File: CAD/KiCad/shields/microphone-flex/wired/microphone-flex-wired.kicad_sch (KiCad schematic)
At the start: 22 parts, among them J1 GND / +5V / OUT, J2 LEFT / 1x05 RIGHT ANGLE, J3 RIGHT / 1x05 RIGHT ANGLE, M1 UP / ONE MODULE ONLY

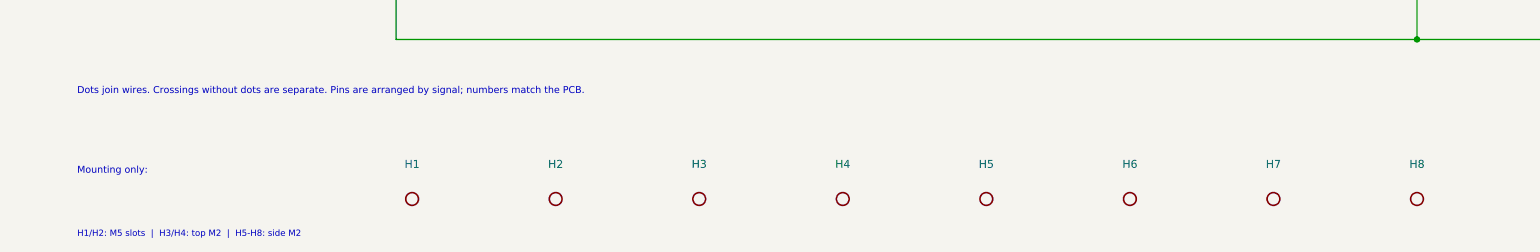
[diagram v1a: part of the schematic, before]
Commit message: Reroute microphone flex around the approved component placement
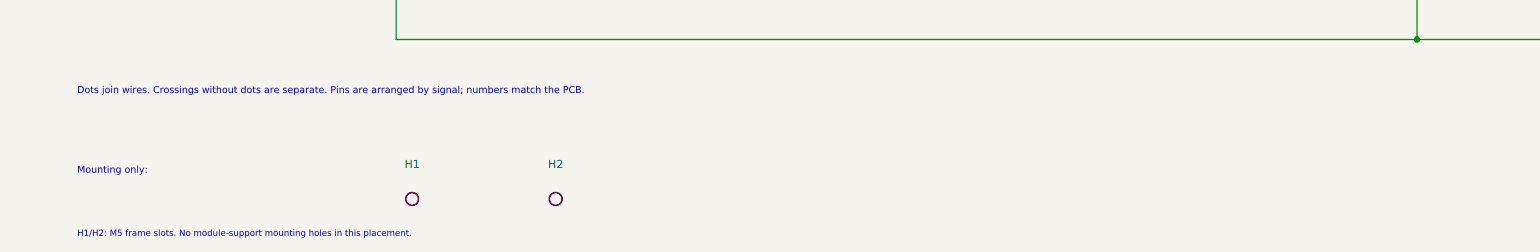
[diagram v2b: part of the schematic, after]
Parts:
- removed H3: M2 MODULE / INSULATING SPACER, Shields:Flex_M2_Top, symbol Colloquy:H3
- removed H4: M2 MODULE / INSULATING SPACER, Shields:Flex_M2_Top, symbol Colloquy:H4
- removed H5: M2 SIDE SUPPORT BASE, Shields:Flex_M2_Base, symbol Colloquy:H5
- removed H6: M2 SIDE SUPPORT BASE, Shields:Flex_M2_Base, symbol Colloquy:H6
- removed H7: M2 SIDE SUPPORT BASE, Shields:Flex_M2_Base, symbol Colloquy:H7
- removed H8: M2 SIDE SUPPORT BASE, Shields:Flex_M2_Base, symbol Colloquy:H8
- J2: footprint Shields:Flex_Socket_Side -> Shields:Flex_Socket_Left_Overhang
- J3: footprint Shields:Flex_Socket_Side -> Shields:Flex_Socket_Right_Overhang
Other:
- note added: "H1/H2: M5 frame slots. No module-support mounting holes in this placement."
- note removed: "H1/H2: M5 slots | H3/H4: top M2 | H5-H8: side M2"
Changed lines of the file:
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@@
 (symbol (lib_id "Colloquy:M1") (at 182.88 68.58 0) (unit 1) (in_bom yes) (on_board yes)(property "Reference" "M1" (at 182.8800 55.4200 0) (effects (font (size 1.27 1.27))  ))(property "Value" "UP / ONE MODULE ONLY" (at 182.8800 68.5800 0) (effects (font (size 1.27 1.27))  (hide yes)))(property "Footprint" "Shields:Flex_Socket_Up" (at 182.8800 68.5800 0) (effects (font (size 1.27 1.27))  (hide yes)))(instances (project "microphone-flex-wired" (path "/cd62561b-1660-5a82-97f3-9afdea717d34" (reference "M1") (unit 1)))))
 (text "UP / vertical" (at 157.48 60.96 0) (effects (font (size 1.27 1.27) ) (justify left top)))
-(symbol (lib_id "Colloquy:J2") (at 261.62 68.58 0) (unit 1) (in_bom yes) (on_board yes)(property "Reference" "J2" (at 261.6200 55.4200 0) (effects (font (size 1.27 1.27))  ))(property "Value" "LEFT / 1x05 RIGHT ANGLE" (at 261.6200 68.5800 0) (effects (font (size 1.27 1.27))  (hide yes)))(property "Footprint" "Shields:Flex_Socket_Side" (at 261.6200 68.5800 0) (effects (font (size 1.27 1.27))  (hide yes)))(instances (project "microphone-flex-wired" (path "/cd62561b-1660-5a82-97f3-9afdea717d34" (reference "J2") (unit 1)))))
+(symbol (lib_id "Colloquy:J2") (at 261.62 68.58 0) (unit 1) (in_bom yes) (on_board yes)(property "Reference" "J2" (at 261.6200 55.4200 0) (effects (font (size 1.27 1.27))  ))(property "Value" "LEFT / 1x05 RIGHT ANGLE" (at 261.6200 68.5800 0) (effects (font (size 1.27 1.27))  (hide yes)))(property "Footprint" "Shields:Flex_Socket_Left_Overhang" (at 261.6200 68.5800 0) (effects (font (size 1.27 1.27))  (hide yes)))(instances (project "microphone-flex-wired" (path "/cd62561b-1660-5a82-97f3-9afdea717d34" (reference "J2") (unit 1)))))
 (text "LEFT / right angle" (at 236.22 60.96 0) (effects (font (size 1.27 1.27) ) (justify left top)))
-(symbol (lib_id "Colloquy:J3") (at 340.36 68.58 0) (unit 1) (in_bom yes) (on_board yes)(property "Reference" "J3" (at 340.3600 55.4200 0) (effects (font (size 1.27 1.27))  ))(property "Value" "RIGHT / 1x05 RIGHT ANGLE" (at 340.3600 68.5800 0) (effects (font (size 1.27 1.27))  (hide yes)))(property "Footprint" "Shields:Flex_Socket_Side" (at 340.3600 68.5800 0) (effects (font (size 1.27 1.27))  (hide yes)))(instances (project "microphone-flex-wired" (path "/cd62561b-1660-5a82-97f3-9afdea717d34" (reference "J3") (unit 1)))))
+(symbol (lib_id "Colloquy:J3") (at 340.36 68.58 0) (unit 1) (in_bom yes) (on_board yes)(property "Reference" "J3" (at 340.3600 55.4200 0) (effects (font (size 1.27 1.27))  ))(property "Value" "RIGHT / 1x05 RIGHT ANGLE" (at 340.3600 68.5800 0) (effects (font (size 1.27 1.27))  (hide yes)))(property "Footprint" "Shields:Flex_Socket_Right_Overhang" (at 340.3600 68.5800 0) (effects (font (size 1.27 1.27))  (hide yes)))(instances (project "microphone-flex-wired" (path "/cd62561b-1660-5a82-97f3-9afdea717d34" (reference "J3") (unit 1)))))
 (text "RIGHT / right angle" (at 314.96 60.96 0) (effects (font (size 1.27 1.27) ) (justify left top)))
 (symbol (lib_id "Colloquy:J1") (at 30.48 142.24 0) (unit 1) (in_bom yes) (on_board yes)(property "Reference" "J1" (at 30.4800 88.4400 0) (effects (font (size 1.27 1.27))  ))(property "Value" "GND / +5V / OUT" (at 30.4800 142.2400 0) (effects (font (size 1.27 1.27))  (hide yes)))(property "Footprint" "Shields:JST_EH_B3B-EH-A_1x03_P2.50mm_Vertical" (at 30.4800 142.2400 0) (effects (font (size 1.27 1.27))  (hide yes)))(instances (project "microphone-flex-wired" (path "/cd62561b-1660-5a82-97f3-9afdea717d34" (reference "J1") (unit 1)))))
@@
 (symbol (lib_id "Colloquy:H1") (at 73.66 274.32 0) (unit 1) (in_bom no) (on_board yes)(property "Reference" "H1" (at 73.6600 268.7800 0) (effects (font (size 1.27 1.27))  ))(property "Value" "M5 SLOT 12x5.5 / TRANSVERSE" (at 73.6600 274.3200 0) (effects (font (size 1.27 1.27))  (hide yes)))(property "Footprint" "Shields:Flex_M5_Slot12x5.5_Keepout" (at 73.6600 274.3200 0) (effects (font (size 1.27 1.27))  (hide yes)))(instances (project "microphone-flex-wired" (path "/cd62561b-1660-5a82-97f3-9afdea717d34" (reference "H1") (unit 1)))))
 (symbol (lib_id "Colloquy:H2") (at 96.52 274.32 0) (unit 1) (in_bom no) (on_board yes)(property "Reference" "H2" (at 96.5200 268.7800 0) (effects (font (size 1.27 1.27))  ))(property "Value" "M5 SLOT 12x5.5 / TRANSVERSE" (at 96.5200 274.3200 0) (effects (font (size 1.27 1.27))  (hide yes)))(property "Footprint" "Shields:Flex_M5_Slot12x5.5_Keepout" (at 96.5200 274.3200 0) (effects (font (size 1.27 1.27))  (hide yes)))(instances (project "microphone-flex-wired" (path "/cd62561b-1660-5a82-97f3-9afdea717d34" (reference "H2") (unit 1)))))
-(symbol (lib_id "Colloquy:H3") (at 119.38 274.32 0) (unit 1) (in_bom no) (on_board yes)(property "Reference" "H3" (at 119.3800 268.7800 0) (effects (font (size 1.27 1.27))  ))(property "Value" "M2 MODULE / INSULATING SPACER" (at 119.3800 274.3200 0) (effects (font (size 1.27 1.27))  (hide yes)))(property "Footprint" "Shields:Flex_M2_Top" (at 119.3800 274.3200 0) (effects (font (size 1.27 1.27))  (hide yes)))(instances (project "microphone-flex-wired" (path "/cd62561b-1660-5a82-97f3-9afdea717d34" (reference "H3") (unit 1)))))
-(symbol (lib_id "Colloquy:H4") (at 142.24 274.32 0) (unit 1) (in_bom no) (on_board yes)(property "Reference" "H4" (at 142.2400 268.7800 0) (effects (font (size 1.27 1.27))  ))(property "Value" "M2 MODULE / INSULATING SPACER" (at 142.2400 274.3200 0) (effects (font (size 1.27 1.27))  (hide yes)))(property "Footprint" "Shields:Flex_M2_Top" (at 142.2400 274.3200 0) (effects (font (size 1.27 1.27))  (hide yes)))(instances (project "microphone-flex-wired" (path "/cd62561b-1660-5a82-97f3-9afdea717d34" (reference "H4") (unit 1)))))
-(symbol (lib_id "Colloquy:H5") (at 165.1 274.32 0) (unit 1) (in_bom no) (on_board yes)(property "Reference" "H5" (at 165.1000 268.7800 0) (effects (font (size 1.27 1.27))  ))(property "Value" "M2 SIDE SUPPORT BASE" (at 165.1000 274.3200 0) (effects (font (size 1.27 1.27))  (hide yes)))(property "Footprint" "Shields:Flex_M2_Base" (at 165.1000 274.3200 0) (effects (font (size 1.27 1.27))  (hide yes)))(instances (project "microphone-flex-wired" (path "/cd62561b-1660-5a82-97f3-9afdea717d34" (reference "H5") (unit 1)))))
-(symbol (lib_id "Colloquy:H6") (at 187.96 274.32 0) (unit 1) (in_bom no) (on_board yes)(property "Reference" "H6" (at 187.9600 268.7800 0) (effects (font (size 1.27 1.27))  ))(property "Value" "M2 SIDE SUPPORT BASE" (at 187.9600 274.3200 0) (effects (font (size 1.27 1.27))  (hide yes)))(property "Footprint" "Shields:Flex_M2_Base" (at 187.9600 274.3200 0) (effects (font (size 1.27 1.27))  (hide yes)))(instances (project "microphone-flex-wired" (path "/cd62561b-1660-5a82-97f3-9afdea717d34" (reference "H6") (unit 1)))))
-(symbol (lib_id "Colloquy:H7") (at 210.82 274.32 0) (unit 1) (in_bom no) (on_board yes)(property "Reference" "H7" (at 210.8200 268.7800 0) (effects (font (size 1.27 1.27))  ))(property "Value" "M2 SIDE SUPPORT BASE" (at 210.8200 274.3200 0) (effects (font (size 1.27 1.27))  (hide yes)))(property "Footprint" "Shields:Flex_M2_Base" (at 210.8200 274.3200 0) (effects (font (size 1.27 1.27))  (hide yes)))(instances (project "microphone-flex-wired" (path "/cd62561b-1660-5a82-97f3-9afdea717d34" (reference "H7") (unit 1)))))
-(symbol (lib_id "Colloquy:H8") (at 233.68 274.32 0) (unit 1) (in_bom no) (on_board yes)(property "Reference" "H8" (at 233.6800 268.7800 0) (effects (font (size 1.27 1.27))  ))(property "Value" "M2 SIDE SUPPORT BASE" (at 233.6800 274.3200 0) (effects (font (size 1.27 1.27))  (hide yes)))(property "Footprint" "Shields:Flex_M2_Base" (at 233.6800 274.3200 0) (effects (font (size 1.27 1.27))  (hide yes)))(instances (project "microphone-flex-wired" (path "/cd62561b-1660-5a82-97f3-9afdea717d34" (reference "H8") (unit 1)))))
-(text "H1/H2: M5 slots  |  H3/H4: top M2  |  H5-H8: side M2" (at 20.32 279.4 0) (effects (font (size 1.0 1.0) ) (justify left top)))
+(text "H1/H2: M5 frame slots. No module-support mounting holes in this placement." (at 20.32 279.4 0) (effects (font (size 1.0 1.0) ) (justify left top)))
 (wire (pts (xy 55.8800 101.6000) (xy 66.0400 101.6000)) (stroke (width 0) (type default)))
 (wire (pts (xy 55.8800 162.5600) (xy 83.8200 162.5600)) (stroke (width 0) (type default)))

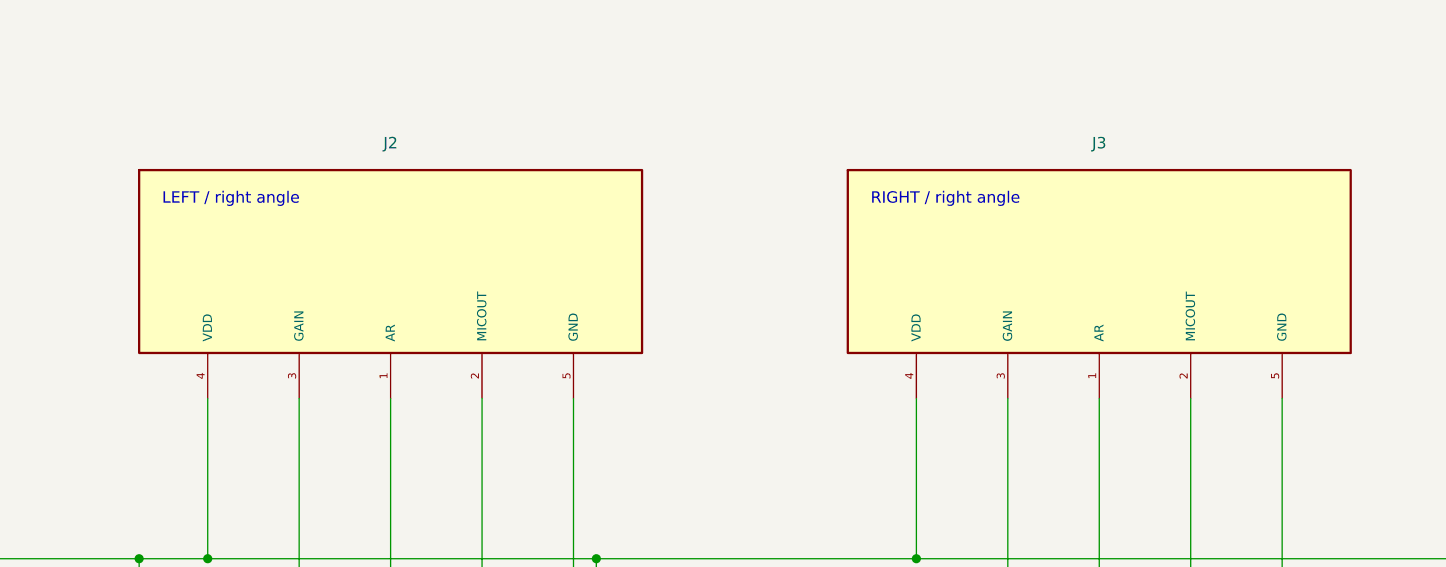
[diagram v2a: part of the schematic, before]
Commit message: Flip side microphones below the carrier and reverse their pin mapping
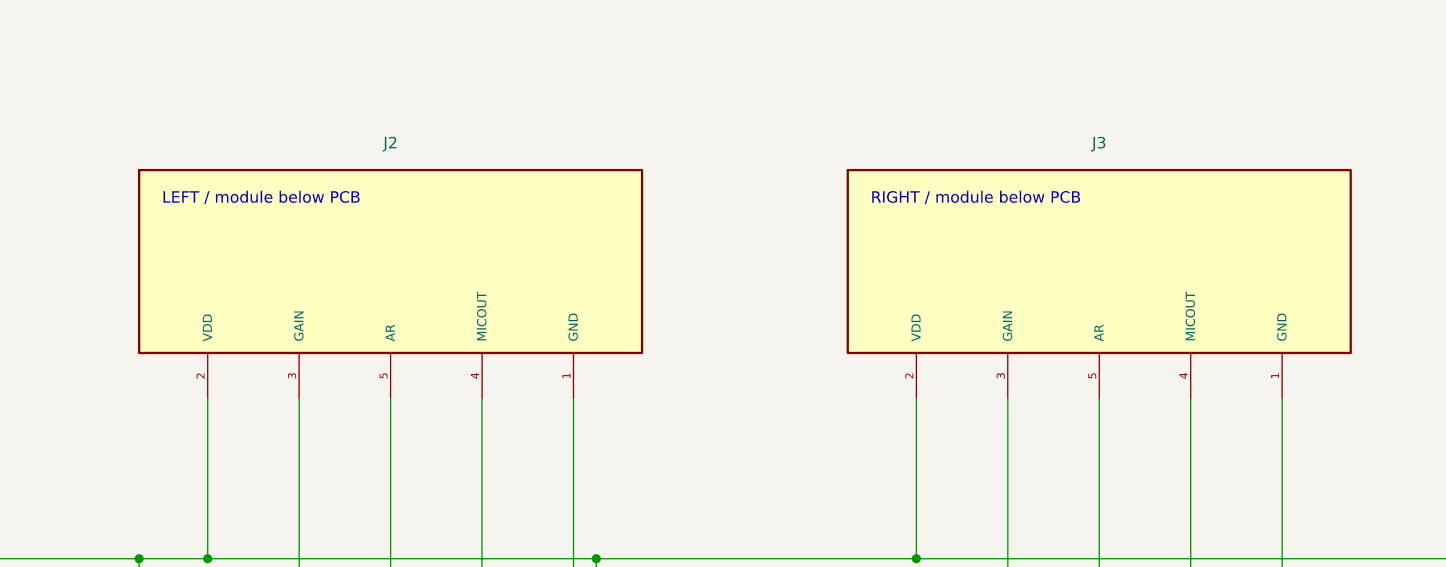
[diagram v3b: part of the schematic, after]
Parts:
- J2: value LEFT / 1x05 RIGHT ANGLE -> LEFT / DOWNWARD MODULE
- J3: value RIGHT / 1x05 RIGHT ANGLE -> RIGHT / DOWNWARD MODULE
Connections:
- net at C6.1, C7.1, JP1.3 (VDD)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: now also J2.2 (VDD), J3.2 (VDD); no longer J2.4 (VDD), J3.4 (VDD)
- net at C6.2, C7.2, D1.1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: now also J2.1 (GND), J3.1 (GND); no longer J2.5 (GND), J3.5 (GND)
- net at M1.4 (Out), R5.1, TP1.1: now also J2.4 (MICOUT), J3.4 (MICOUT); no longer J2.2 (MICOUT), J3.2 (MICOUT)
- net at JP2.2 (AR), M1.5 (AR): now also J2.5 (AR), J3.5 (AR); no longer J2.1 (AR), J3.1 (AR)
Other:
- note added: "LEFT / module below PCB"
- note added: "RIGHT / module below PCB"
- note removed: "LEFT / right angle"
- note removed: "RIGHT / right angle"
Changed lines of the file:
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@@
 (symbol (lib_id "Colloquy:M1") (at 182.88 68.58 0) (unit 1) (in_bom yes) (on_board yes)(property "Reference" "M1" (at 182.8800 55.4200 0) (effects (font (size 1.27 1.27))  ))(property "Value" "UP / ONE MODULE ONLY" (at 182.8800 68.5800 0) (effects (font (size 1.27 1.27))  (hide yes)))(property "Footprint" "Shields:Flex_Socket_Up" (at 182.8800 68.5800 0) (effects (font (size 1.27 1.27))  (hide yes)))(instances (project "microphone-flex-wired" (path "/cd62561b-1660-5a82-97f3-9afdea717d34" (reference "M1") (unit 1)))))
 (text "UP / vertical" (at 157.48 60.96 0) (effects (font (size 1.27 1.27) ) (justify left top)))
-(symbol (lib_id "Colloquy:J2") (at 261.62 68.58 0) (unit 1) (in_bom yes) (on_board yes)(property "Reference" "J2" (at 261.6200 55.4200 0) (effects (font (size 1.27 1.27))  ))(property "Value" "LEFT / 1x05 RIGHT ANGLE" (at 261.6200 68.5800 0) (effects (font (size 1.27 1.27))  (hide yes)))(property "Footprint" "Shields:Flex_Socket_Left_Overhang" (at 261.6200 68.5800 0) (effects (font (size 1.27 1.27))  (hide yes)))(instances (project "microphone-flex-wired" (path "/cd62561b-1660-5a82-97f3-9afdea717d34" (reference "J2") (unit 1)))))
-(text "LEFT / right angle" (at 236.22 60.96 0) (effects (font (size 1.27 1.27) ) (justify left top)))
-(symbol (lib_id "Colloquy:J3") (at 340.36 68.58 0) (unit 1) (in_bom yes) (on_board yes)(property "Reference" "J3" (at 340.3600 55.4200 0) (effects (font (size 1.27 1.27))  ))(property "Value" "RIGHT / 1x05 RIGHT ANGLE" (at 340.3600 68.5800 0) (effects (font (size 1.27 1.27))  (hide yes)))(property "Footprint" "Shields:Flex_Socket_Right_Overhang" (at 340.3600 68.5800 0) (effects (font (size 1.27 1.27))  (hide yes)))(instances (project "microphone-flex-wired" (path "/cd62561b-1660-5a82-97f3-9afdea717d34" (reference "J3") (unit 1)))))
-(text "RIGHT / right angle" (at 314.96 60.96 0) (effects (font (size 1.27 1.27) ) (justify left top)))
+(symbol (lib_id "Colloquy:J2") (at 261.62 68.58 0) (unit 1) (in_bom yes) (on_board yes)(property "Reference" "J2" (at 261.6200 55.4200 0) (effects (font (size 1.27 1.27))  ))(property "Value" "LEFT / DOWNWARD MODULE" (at 261.6200 68.5800 0) (effects (font (size 1.27 1.27))  (hide yes)))(property "Footprint" "Shields:Flex_Socket_Left_Overhang" (at 261.6200 68.5800 0) (effects (font (size 1.27 1.27))  (hide yes)))(instances (project "microphone-flex-wired" (path "/cd62561b-1660-5a82-97f3-9afdea717d34" (reference "J2") (unit 1)))))
+(text "LEFT / module below PCB" (at 236.22 60.96 0) (effects (font (size 1.27 1.27) ) (justify left top)))
+(symbol (lib_id "Colloquy:J3") (at 340.36 68.58 0) (unit 1) (in_bom yes) (on_board yes)(property "Reference" "J3" (at 340.3600 55.4200 0) (effects (font (size 1.27 1.27))  ))(property "Value" "RIGHT / DOWNWARD MODULE" (at 340.3600 68.5800 0) (effects (font (size 1.27 1.27))  (hide yes)))(property "Footprint" "Shields:Flex_Socket_Right_Overhang" (at 340.3600 68.5800 0) (effects (font (size 1.27 1.27))  (hide yes)))(instances (project "microphone-flex-wired" (path "/cd62561b-1660-5a82-97f3-9afdea717d34" (reference "J3") (unit 1)))))
+(text "RIGHT / module below PCB" (at 314.96 60.96 0) (effects (font (size 1.27 1.27) ) (justify left top)))
 (symbol (lib_id "Colloquy:J1") (at 30.48 142.24 0) (unit 1) (in_bom yes) (on_board yes)(property "Reference" "J1" (at 30.4800 88.4400 0) (effects (font (size 1.27 1.27))  ))(property "Value" "GND / +5V / OUT" (at 30.4800 142.2400 0) (effects (font (size 1.27 1.27))  (hide yes)))(property "Footprint" "Shields:JST_EH_B3B-EH-A_1x03_P2.50mm_Vertical" (at 30.4800 142.2400 0) (effects (font (size 1.27 1.27))  (hide yes)))(instances (project "microphone-flex-wired" (path "/cd62561b-1660-5a82-97f3-9afdea717d34" (reference "J1") (unit 1)))))
 (symbol (lib_id "Colloquy:R4") (at 88.9 101.6 0) (unit 1) (in_bom yes) (on_board yes)(property "Reference" "R4" (at 88.9000 97.5840 0) (effects (font (size 1.27 1.27))  ))(property "Value" "33R" (at 88.9000 101.6000 0) (effects (font (size 1.27 1.27))  (hide yes)))(property "Footprint" "Shields:R_0603_1608Metric" (at 88.9000 101.6000 0) (effects (font (size 1.27 1.27))  (hide yes)))(instances (project "microphone-flex-wired" (path "/cd62561b-1660-5a82-97f3-9afdea717d34" (reference "R4") (unit 1)))))
